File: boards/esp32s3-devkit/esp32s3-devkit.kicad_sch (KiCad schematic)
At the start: 37 parts, among them J1 Conn_01x17_Pin, J2 Conn_01x17_Pin, J3 USB_C_Receptacle_USB2.0_16P, Q1 Q_PMOS_GSD, SW1 MK-12C03-G015, SW2 RESET, SW3 BOOT, U1 TPS63070RNMR, U2 ESP32-S3-WROOM-1, U3 USBLC6-2SC6

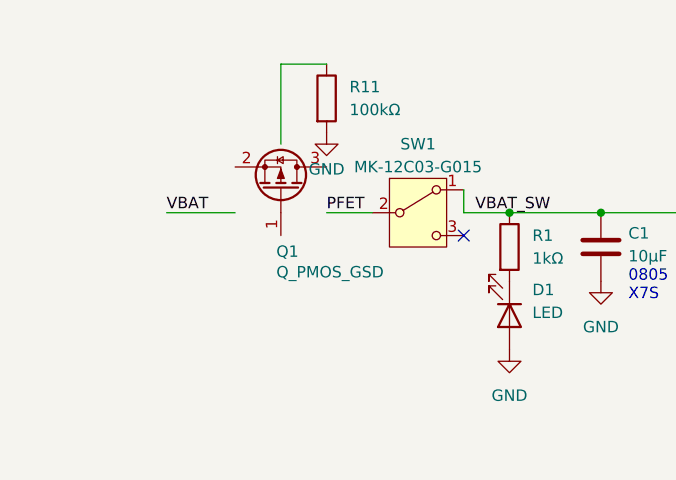
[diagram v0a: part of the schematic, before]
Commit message: fix(esp32s3-devkit): rewire Q1 S/D swap with explicit wires instead of mirror
The (mirror x) transform moved Q1's pins off their wires, breaking the
netlist (5 ERC errors, 8 parity warnings). Replace with deterministic
rewiring: drop the mirror, keep Q1 at its original orientation, and
swap the wire connections so drain goes to VBAT and source to SW1
(PFET net). Matches the PCB pad nets from the previous commit; no
layout change needed.
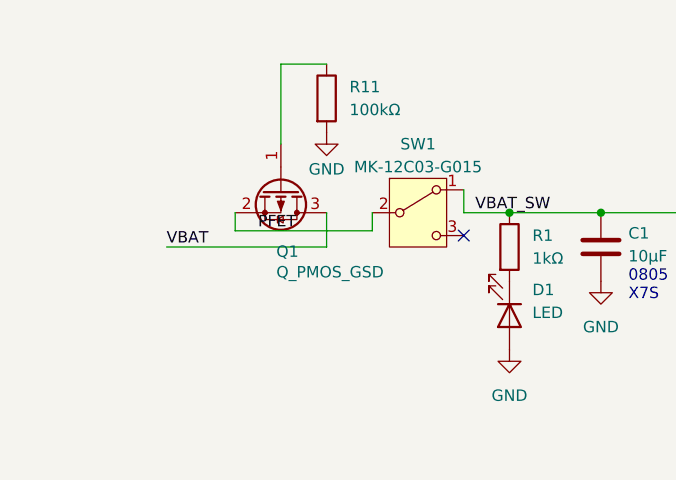
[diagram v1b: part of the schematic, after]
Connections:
- net PFET: now also Q1.2 (S)
- net VBAT: now also Q1.3 (D)
- net at R11.1: now also Q1.1 (G)
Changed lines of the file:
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@@
 	(wire
 		(pts
+			(xy 52.07 46.99) (xy 52.07 50.8)
+		)
+		(stroke
+			(width 0)
+			(type default)
+		)
+	)
+	(wire
+		(pts
+			(xy 52.07 50.8) (xy 34.29 50.8)
+		)
+		(stroke
+			(width 0)
+			(type default)
+		)
+	)
+	(wire
+		(pts
+			(xy 41.91 46.99) (xy 41.91 49.0)
+		)
+		(stroke
+			(width 0)
+			(type default)
+		)
+	)
+	(wire
+		(pts
+			(xy 41.91 49.0) (xy 57.15 49.0)
+		)
+		(stroke
+			(width 0)
+			(type default)
+		)
+	)
+	(wire
+		(pts
+			(xy 57.15 49.0) (xy 57.15 46.99)
+		)
+		(stroke
+			(width 0)
+			(type default)
+		)
+	)
+	(wire
+		(pts
 			(xy 104.14 124.46) (xy 106.68 124.46)
 		)
@@
 	(wire
 		(pts
-			(xy 52.07 46.99) (xy 57.15 46.99)
-		)
-		(stroke
-			(width 0)
-			(type default)
-		)
-	)
-	(wire
-		(pts
 			(xy 187.96 120.65) (xy 187.96 127)
 		)
@@
 	(wire
 		(pts
-			(xy 34.29 46.99) (xy 41.91 46.99)
-		)
-		(stroke
-			(width 0)
-			(type default)
-		)
-	)
-	(wire
-		(pts
 			(xy 66.04 157.48) (xy 73.66 157.48)
 		)
@@
 	)
 	(label "VBAT"
-		(at 34.29 46.99 0)
+		(at 34.29 50.8 0)
 		(effects
 			(font
@@
 	)
 	(label "PFET"
-		(at 52.07 46.99 0)
+		(at 44.45 49.0 0)
 		(effects
 			(font
@@
 		(lib_id "Transistor_FET:Q_PMOS_GSD")
 		(at 46.99 44.45 270)
-		(mirror x)
 		(unit 1)
 		(body_style 1)
